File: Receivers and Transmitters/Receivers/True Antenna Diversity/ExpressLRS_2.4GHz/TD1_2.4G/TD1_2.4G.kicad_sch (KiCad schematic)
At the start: 8 parts, among them J1 Conn_01x04_Pin, J2 Conn_01x04_Socket, U1 TPS7A4701xRGW

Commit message: Updated schematics for TD1_2.4G receiver: ESP32, SX1280, and RFX2401C blocks
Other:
- company: https://github.com/Paschalis | TeodoraMiu -> https://github.com/Paschalis
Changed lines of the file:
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@@
 		(date "2025-02-23")
 		(rev "1.0")
-		(company "https://github.com/Paschalis | TeodoraMiu")
+		(company "https://github.com/Paschalis")
 		(comment 3 "The receiver utilizes two independent Semtech LoRa chips.")
 	)
@@
 			"AAAAAAAAAAAAAAAAAAAAAAAAAAAAAAAAAAAAAAAAAAAAAAAAAAAAAAAAAAAAAAAAAAAAAAAAAAAA"
 			"AAAAAAAAAAAAAAAAAAAAAAAAAAAAAAAAAAAAAAAAAAAAAAAAAAAAAAAAAAAAAAAAAAAAAAAAAAAA"
+			"AAAAAAAAAAAAAAAAAAAAAAAAAAAAAAAAAAAAAAAAAAAAAAAAAAAAAAAAAAAAAAAAAAAAAAAAAAAA"
+			"AAAAAAAAAAAAAAAAAAAAAAAAAAAAAAAAAAAAAAAAAAAAAAAAAAAAAAAAAAAAAAAAAAAAAAAAAAAA"
+			"AAAAAAAAAAAAAAAAAAAAAAAAAAAAAAAAAAAAAAAAAAAAAAAAAAAAAAAAAAAAAAAAAAAAAAAAAAAA"
+			"AAAAAAAAAAAAAAAAAAAAAAAAAAAAAAAAAAAAAAAAAAAAAAAAAAAAAAAAAAAAAAAAAAAAAAAAAAAA"
+			"AAAAAAAAAAAAAAAAAAAAAAAAAAAAAAAAAAAAAAAAAAAAAAAAAAAAAAAAAAAAAAAAAAAAAAAAAAAA"
+			"AAAAAAAAAAAAAAAAAAAAAAAAAAAAAAAAAAAAAAAAAAAAAAAAAAAAAAAAAAAAAAAAAAAAAAAAAAAA"
+			"AAAAAAAAAAAAAAAAAAAAAAAAAAAAAAAAAAAAAAAAAAAAAAAAAAAAAAAAAAAAAAAAAAAAAAAAAAAA"
+			"AAAAAAAAAAAAAAAAAAAAAAAAAAAAAAAAAAAAAAAAAAAAAAAAAAAAAAAAAAAAAAAAAAAAAAAAAAAA"
+			"AAAAAAAAAAAAAAAAAAAAAAAAAAAAAAAAAAAAAAAAAAAAAAAAAAAAAAAAAAAAAAAAAAAAAAAAAAAA"
+			"AAAAAAAAAAAAAAAAAAAAAAAAAAAAAAAAAAAAAAAAAAAAAAAAAAAAAAAAAAAAAAAAAAAAAAAAAAAA"
+			"AAAAAAAAAAAAAAAAAAAAAAAAAAAAAAAAAAAAAAAAAAAAAAAAAAAAAAAAAAAAAAAAAAAAAAAAAAAA"
+			"AAAAAAAAAAAAAAAAAAAAAAAAAAAAAAAAAAAAAAAAAAAAAAAAAAAAAAAAAAAAAAAAAAAAAAAAAAAA"
+			"AAAAAAAAAAAAAAAAAAAAAAAAAAAAAAAAAAAAAAAAAAAAAAAAAAAAAAAAAAAAAAAAAAAAAAAAAAAA"
+			"AAAAAAAAAAAAAAAAAAAAAAAAAAAAAAAAAAAAAAAAAAAAAAAAAAAAAAAAAAAAAAAAAAAAAAAAAAAA"
+			"AAAAAAAAAAAAAAAAAAAAAAAAAAAAAAAAAAAAAAAAAAAAAAAAAAAAAAAAAAAAAAAAAAAAAAAAAAAA"
+			"AAAAAAAAAAAAAAAAAAAAAAAAAAAAAAAAAAAAAAAAAAAAAAAAAAAAAAAAAAAAAAAAAAAAAAAAAAAA"
+			"AAAAAAAAAAAAAAAAAAAAAAAAAAAAAAAAAAAAAAAAAAAAAAAAAAAAAAAAAAAAAAAAAAAAAAAAAAAA"
+			"AAAAAAAAAAAAAAAAAAAAAAAAAAAAAAAAAAAAAAAAAAAAAAAAAAAAAAAAAAAAAAAAAAAAAAAAAAAA"

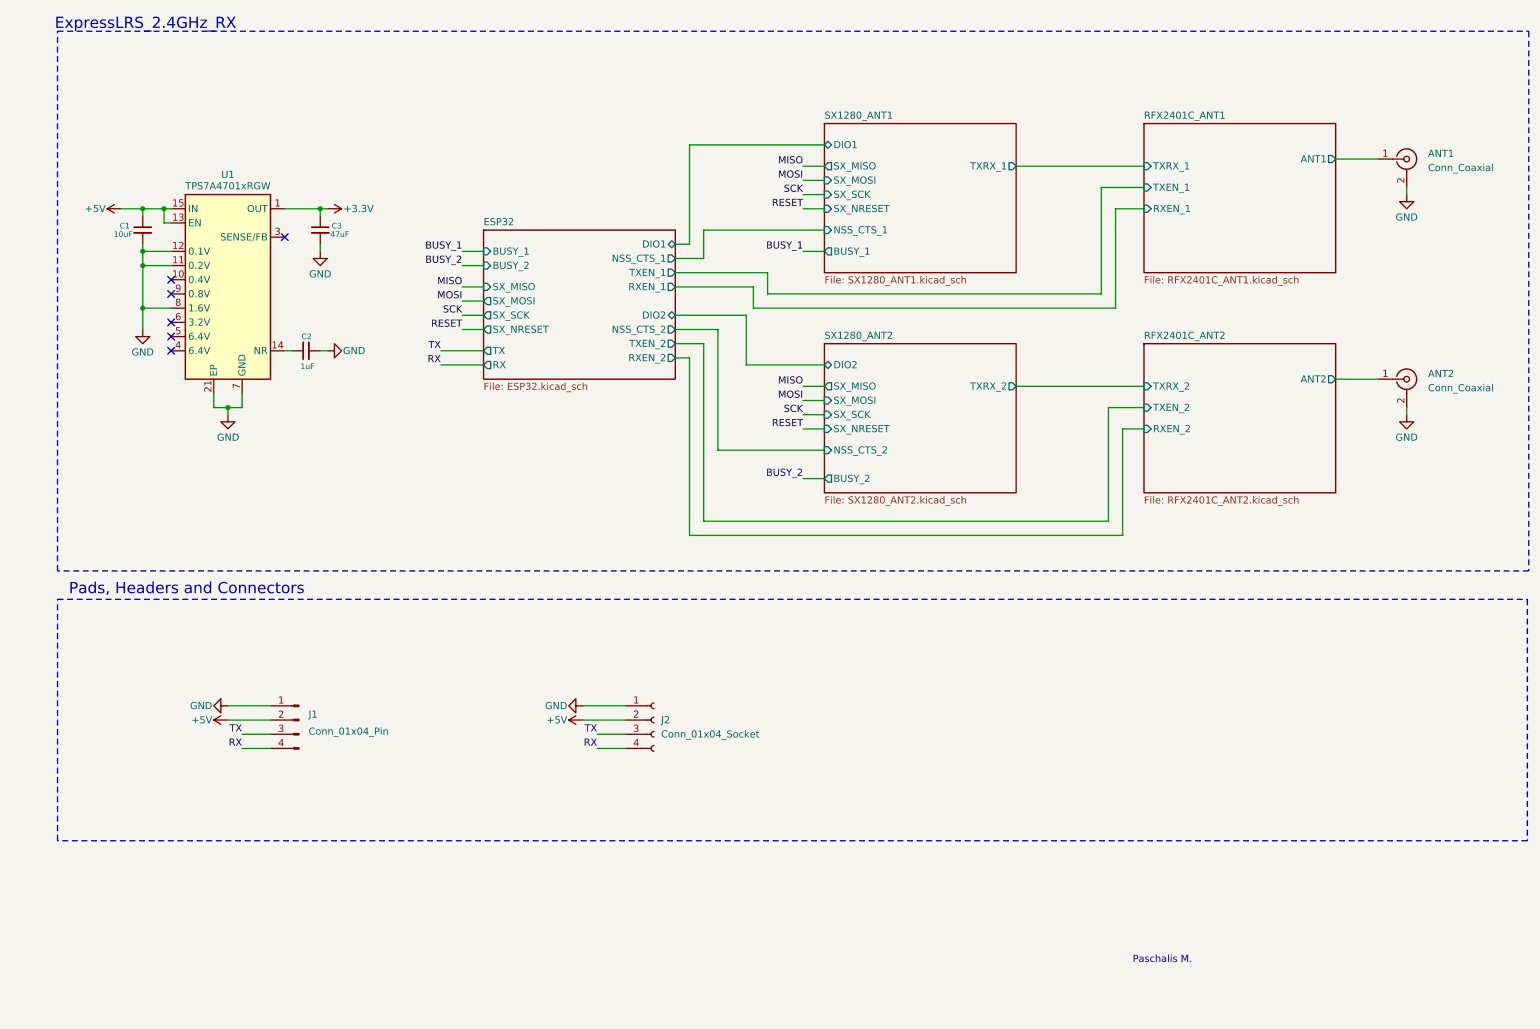
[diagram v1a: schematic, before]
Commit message: Update Antenna Diversity (AD1_2.4G), True Antenna Diversity (TD1_2.4G), and Gemini Mode transmitter (G_TX1): Modify KiCad files, add BOMs and production files; update images, docs, videos, and README; remove outdated Mechanical CAD file
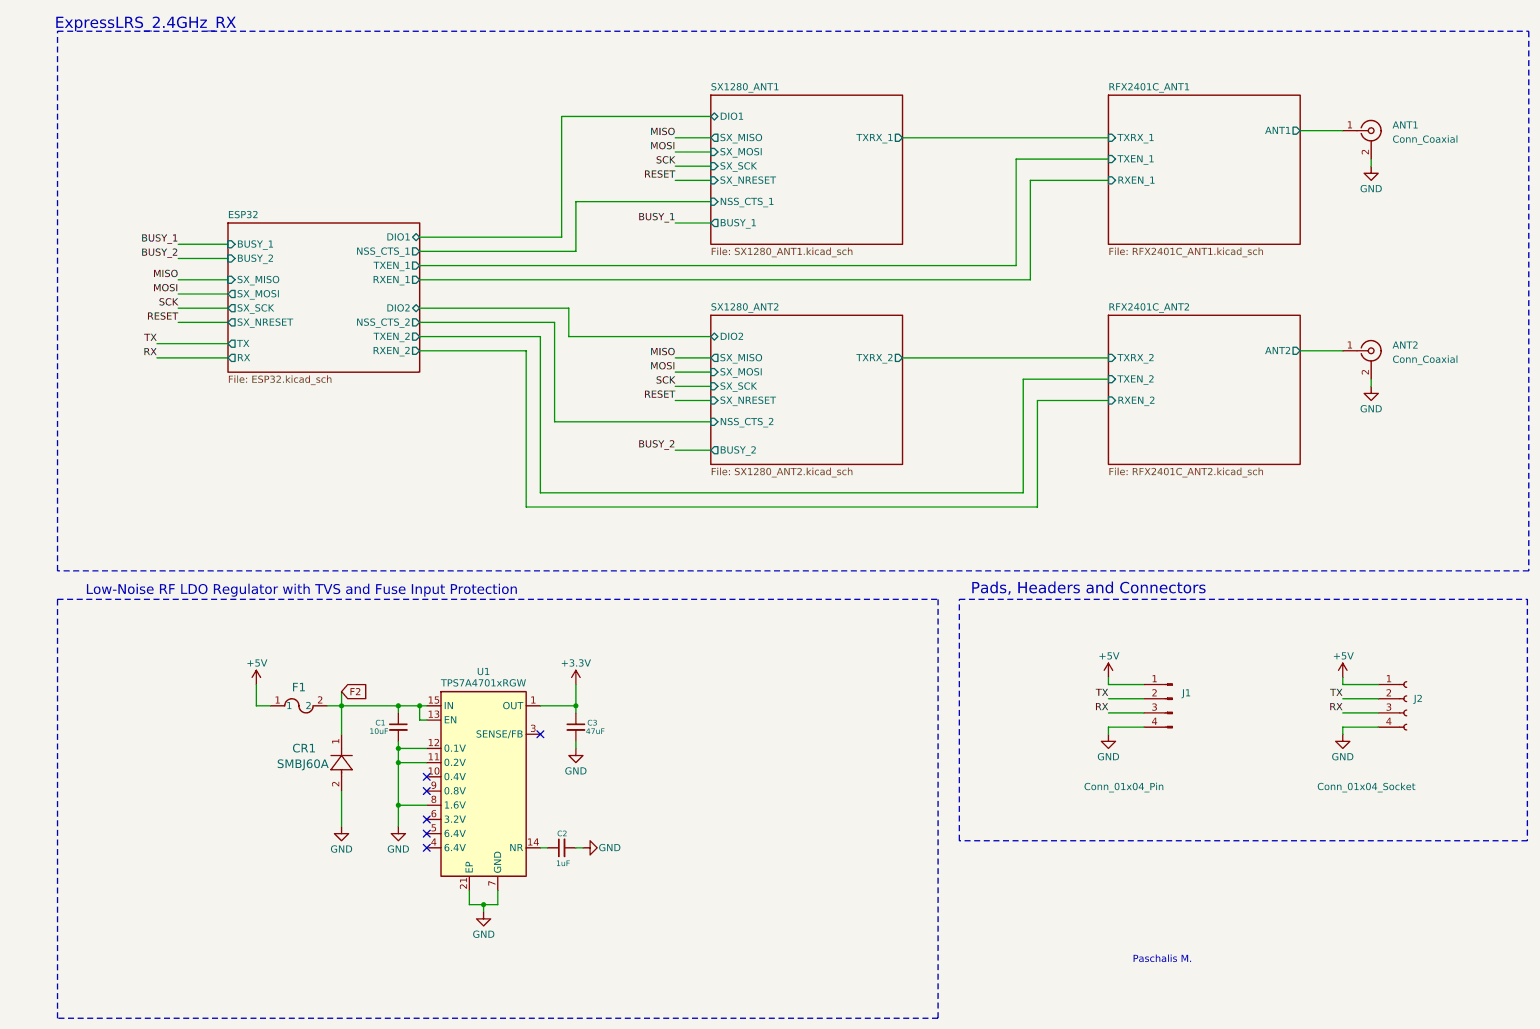
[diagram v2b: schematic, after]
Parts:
- added CR1: SMBJ60A, ul_SMBJ60A:SMBJSeries_LTF, symbol ul_SMBJ60A:SMBJ60A
- added F1: MF-PSMF020X-2, ul_MF-PSMF020X-2:FUSE_F020X_BRN, symbol ul_MF-PSMF020X-2:MF-PSMF020X-2
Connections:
- net +5V: now also J1.1 (Pin_1), J2.1 (Pin_1), F1.1; no longer C1.1, J1.2 (Pin_2), J2.2 (Pin_2), U1.13 (EN), U1.15 (IN), U1.16 (IN)
- net GND: now also J1.4 (Pin_4), J2.4 (Pin_4), CR1.2; no longer J1.1 (Pin_1), J2.1 (Pin_1)
- net RX: now also J1.3 (Pin_3), J2.3 (Pin_3); no longer J1.4 (Pin_4), J2.4 (Pin_4)
- net TX: now also J1.2 (Pin_2), J2.2 (Pin_2); no longer J1.3 (Pin_3), J2.3 (Pin_3)
- new net F2: C1.1, CR1.1, F1.2, U1.13 (EN), U1.15 (IN), U1.16 (IN)
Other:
- note added: "Low-Noise RF LDO Regulator with TVS and Fuse Input Protection"
- moved on the sheet: ANT1, ANT2, C1, C2, C3, J1, J2, U1

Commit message: Update TD1_2.4G: schematic and PCB revisions, BOM export, README; remove old PCBWay production files
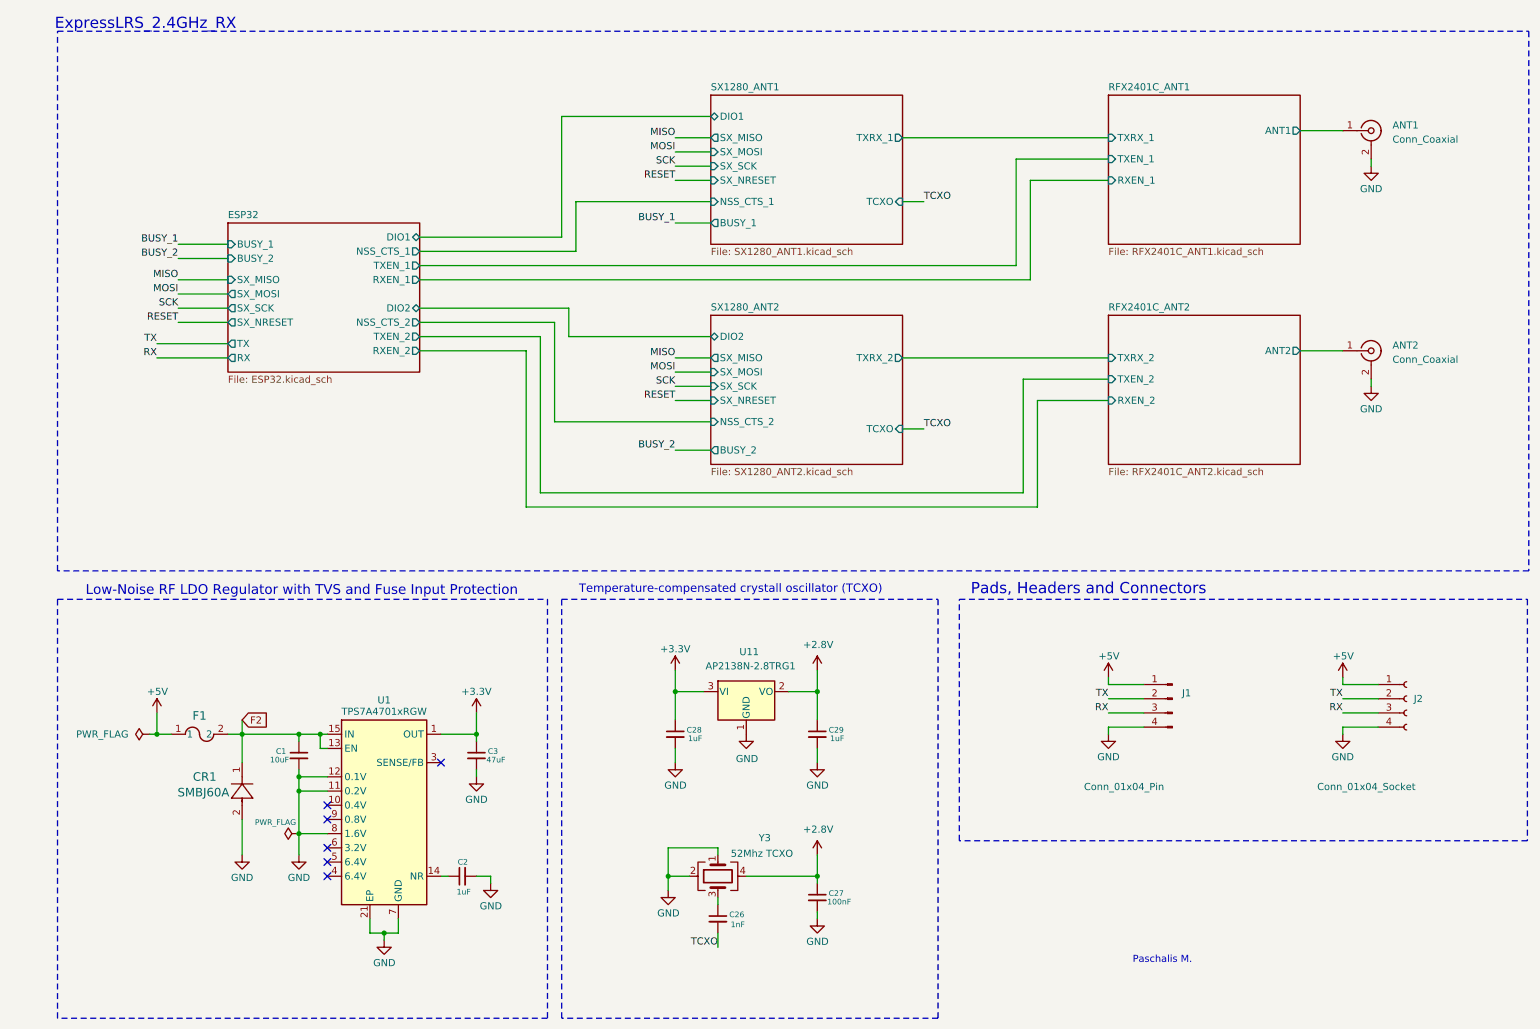
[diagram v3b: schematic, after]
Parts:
- added C26: 1nF, Capacitor_SMD:C_0603_1608Metric_Pad1.08x0.95mm_HandSolder, symbol Device:C_Small
- added C27: 100nF, Capacitor_SMD:C_0603_1608Metric_Pad1.08x0.95mm_HandSolder, symbol Device:C_Small
- added C28, C29: 1uF, Capacitor_SMD:C_0603_1608Metric_Pad1.08x0.95mm_HandSolder, symbol Device:C_Small
- added U11: AP2138N-2.8TRG1, Package_TO_SOT_SMD:SOT-23, symbol Regulator_Linear:AP2127N-2.8
- added Y3: 52Mhz TCXO, Crystal:Crystal_SMD_2016-4Pin_2.0x1.6mm, symbol Device:Crystal_GND24
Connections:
- net +3.3V: now also C28.1, U11.3 (VI)
- net GND: now also C27.2, C28.2, C29.2, U11.1 (GND), Y3.1, Y3.2
- new net: C26.1, Y3.3
- new net +2.8V: C27.1, C29.1, U11.2 (VO), Y3.4
- new net TCXO: C26.2
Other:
- sheet SX1280_ANT1 ports: added TCXO; removed none
- sheet SX1280_ANT2 ports: added TCXO; removed none
- note added: "Temperature-compensated crystall oscillator (TCXO)"
- moved on the sheet: C1, C2, C3, CR1, F1, U1
